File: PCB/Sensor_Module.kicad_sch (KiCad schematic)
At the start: 36 parts, among them J1 Conn_01x02_Pin, J2 Conn_01x01_Pin, J3 Conn_01x02_Pin, J4 Conn_01x02_Pin, J5 Conn_01x02_Pin, Q3 BSS123, Q4 BSS123, Q5 BSS123

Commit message: Changed Sensor Sheet Description
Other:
- company: (none) -> University of Cape Town
- title: (none) -> Sensor Module
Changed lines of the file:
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@@
 (kicad_sch (version 20230121) (generator eeschema)
   (paper "A4")
+  (title_block
+    (title "Sensor Module")
+    (date "2023-03-12")
+    (company "University of Cape Town")
+    (comment 1 "Author: Simon Carthew")
+    (comment 2 "v0.0")
+  )
   (junction (at 162.56 62.23) (diameter 0) (color 0 0 0 0)
   )

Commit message: Merging Fixed
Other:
- note added: "BI-DIRECTIONAL LOGIC LEVEL SHIFTING"
- moved on the sheet: C?, J2, J5, R?, U?

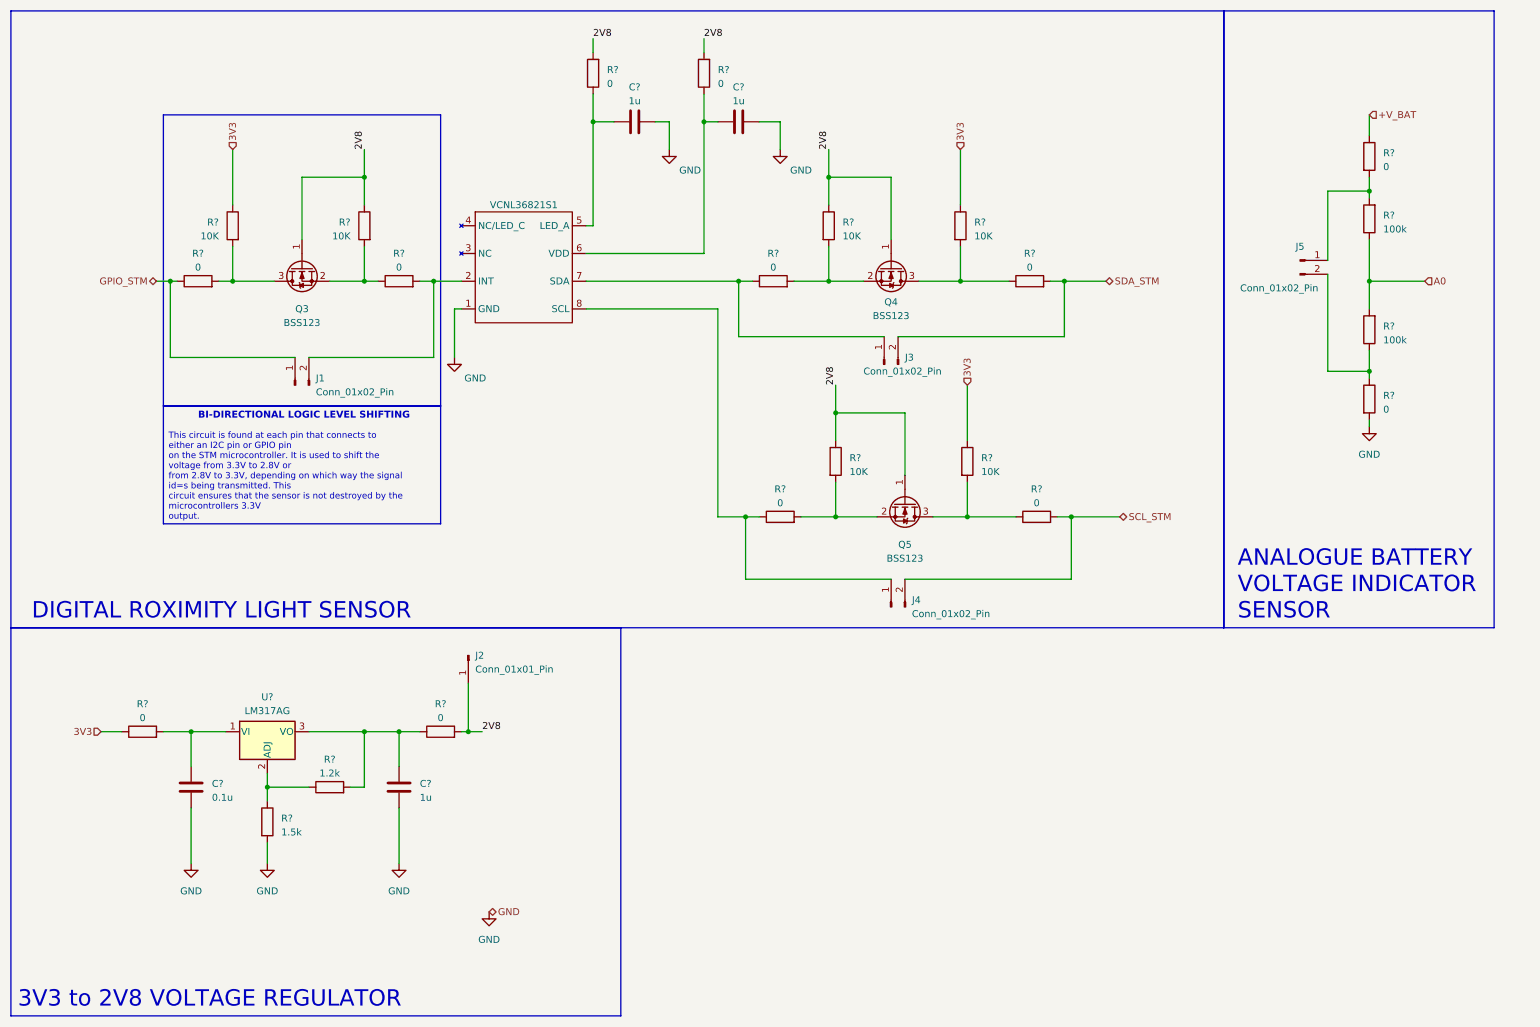
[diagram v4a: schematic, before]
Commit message: Changed Sensor and added hierachiel sheet
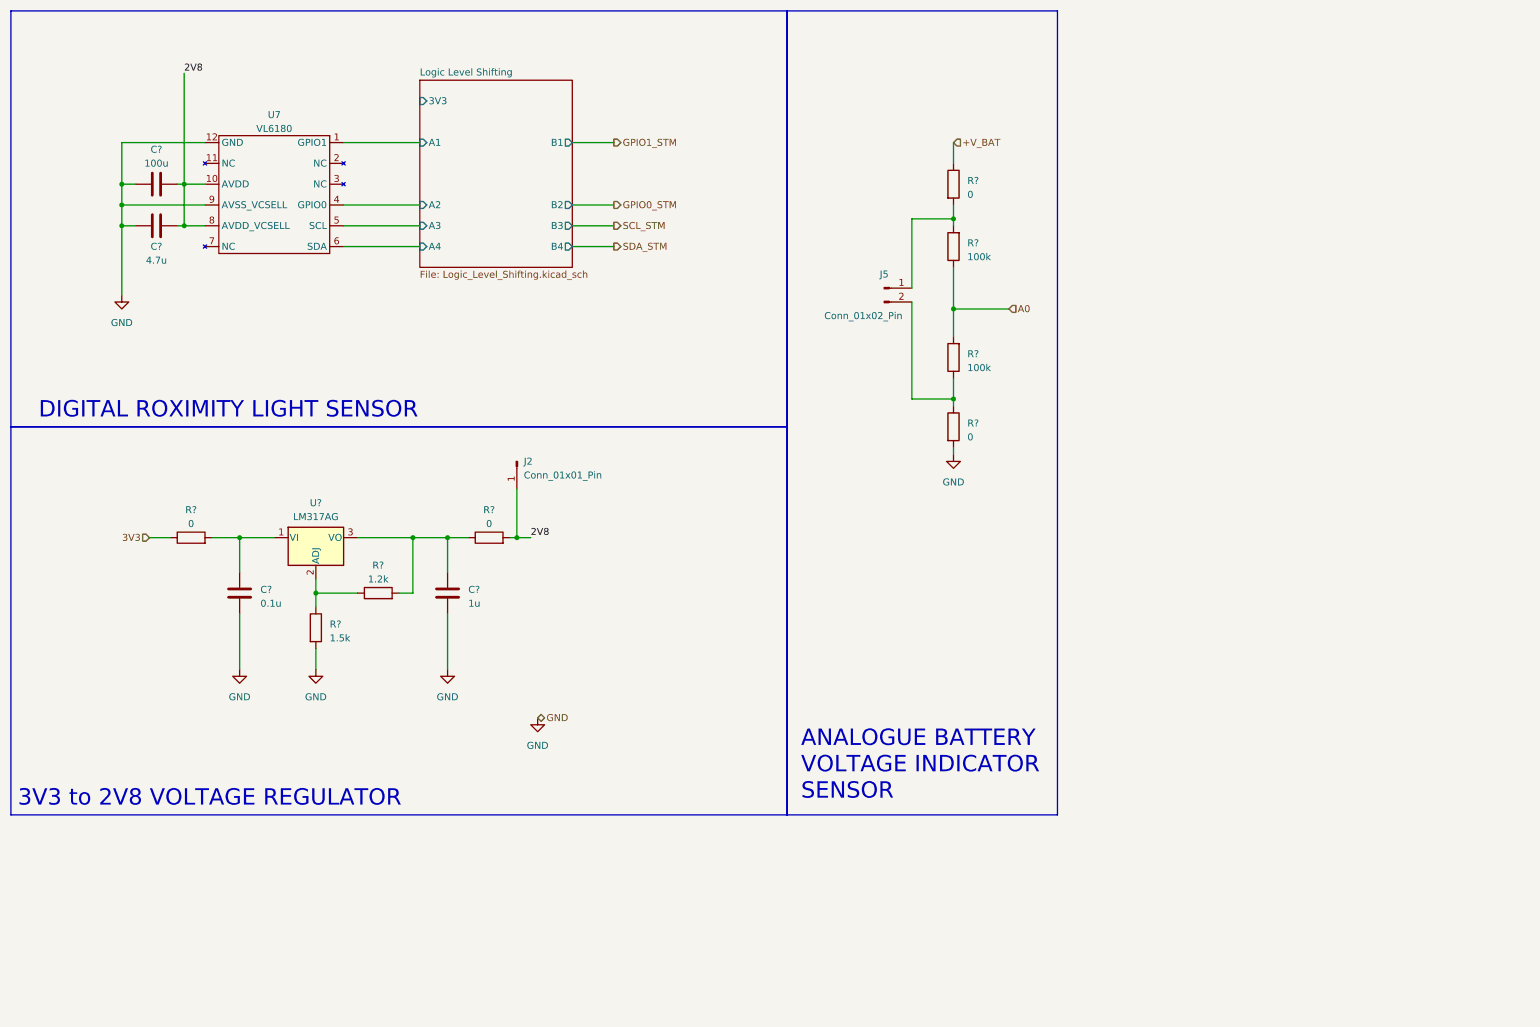
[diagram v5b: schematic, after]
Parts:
- removed C? (x2): 1u, symbol Device:C
- removed J1, J3, J4: Conn_01x02_Pin, symbol Connector:Conn_01x02_Pin
- removed Q3, Q4, Q5: BSS123, Package_TO_SOT_SMD:SOT-23, symbol Transistor_FET:BSS123
- removed R? (x6): 10K, symbol Device:R
- removed R? (x8): 0, symbol Device:R
- removed VCNL36821S1: ~, symbol Proximity Sensor:VCNL36821S
- added C?: 100u, symbol Device:C
- added C?: 4.7u, symbol Device:C
- added U7: VL6180, symbol Proximity Sensor:VL6180
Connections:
- net 2V8: now also C?.1, C?.1, U7.10 (AVDD), U7.8 (AVDD_VCSELL)
- net GND: now also C?.2, C?.2, U7.12 (GND), U7.9 (AVSS_VCSELL)
- new net Logic Level Shifting/A1: U7.1 (GPIO1)
- new net Logic Level Shifting/A2: U7.4 (GPIO0)
- new net Logic Level Shifting/A3: U7.5 (SCL)
- new net Logic Level Shifting/A4: U7.6 (SDA)
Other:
- added sheet Logic Level Shifting (Logic_Level_Shifting.kicad_sch)
- note removed: "BI-DIRECTIONAL LOGIC LEVEL SHIFTING"
- moved on the sheet: C?, J2, J5, R?, U?

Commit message: Merging commit
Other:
- moved on the sheet: J5, R?
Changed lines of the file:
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@@
     (comment 2 "v0.0")
   )
-  (junction (at 185.42 67.31) (diameter 0) (color 0 0 0 0)
+  (junction (at 184.15 85.09) (diameter 0) (color 0 0 0 0)
   )
   (junction (at 44.45 44.45) (diameter 0) (color 0 0 0 0)
@@
   (junction (at 33.02 48.26) (diameter 0) (color 0 0 0 0)
   )
-  (junction (at 185.42 50.8) (diameter 0) (color 0 0 0 0)
-  )
-  (junction (at 185.42 83.82) (diameter 0) (color 0 0 0 0)
+  (junction (at 184.15 68.58) (diameter 0) (color 0 0 0 0)
+  )
+  (junction (at 184.15 101.6) (diameter 0) (color 0 0 0 0)
   )
   (junction (at 44.45 52.07) (diameter 0) (color 0 0 0 0)
@@
     (stroke (width 0) (type default))
   )
-  (wire (pts (xy 185.42 83.82) (xy 185.42 85.09))
+  (wire (pts (xy 184.15 101.6) (xy 184.15 102.87))
     (stroke (width 0) (type default))
   )
@@
     (stroke (width 0) (type default))
   )
-  (wire (pts (xy 185.42 59.69) (xy 185.42 67.31))
+  (wire (pts (xy 184.15 77.47) (xy 184.15 85.09))
     (stroke (width 0) (type default))
   )
@@
     (stroke (width 0) (type default))
   )
-  (wire (pts (xy 177.8 50.8) (xy 177.8 63.5))
-    (stroke (width 0) (type default))
-  )
-  (wire (pts (xy 177.8 83.82) (xy 177.8 66.04))
+  (wire (pts (xy 176.53 68.58) (xy 176.53 81.28))
+    (stroke (width 0) (type default))
+  )
+  (wire (pts (xy 176.53 101.6) (xy 176.53 83.82))
     (stroke (width 0) (type default))
   )
@@
     (stroke (width 0) (type default))
   )
-  (wire (pts (xy 185.42 48.26) (xy 185.42 50.8))
+  (wire (pts (xy 184.15 66.04) (xy 184.15 68.58))
     (stroke (width 0) (type default))
   )
@@
     (stroke (width 0) (type default))
   )
-  (wire (pts (xy 185.42 67.31) (xy 185.42 72.39))
+  (wire (pts (xy 184.15 85.09) (xy 184.15 90.17))
     (stroke (width 0) (type default))
   )
@@
     (stroke (width 0) (type default))
   )
+  (wire (pts (xy 80.01 22.86) (xy 80.01 29.21))
+    (stroke (width 0) (type default))
+  )
+  (wire (pts (xy 87.63 29.21) (xy 80.01 29.21))
+    (stroke (width 0) (type default))
+  )
   (wire (pts (xy 68.58 119.38) (xy 68.58 121.92))
     (stroke (width 0) (type default))
   )
-  (wire (pts (xy 185.42 50.8) (xy 185.42 52.07))
+  (wire (pts (xy 184.15 68.58) (xy 184.15 69.85))
     (stroke (width 0) (type default))
   )
@@
     (stroke (width 0) (type default))
   )
-  (wire (pts (xy 185.42 83.82) (xy 177.8 83.82))
-    (stroke (width 0) (type default))
-  )
-  (wire (pts (xy 185.42 67.31) (xy 195.58 67.31))
+  (wire (pts (xy 184.15 101.6) (xy 176.53 101.6))
+    (stroke (width 0) (type default))
+  )
+  (wire (pts (xy 184.15 85.09) (xy 194.31 85.09))
     (stroke (width 0) (type default))
   )
@@
     (stroke (width 0) (type default))
   )
-  (wire (pts (xy 185.42 80.01) (xy 185.42 83.82))
+  (wire (pts (xy 184.15 97.79) (xy 184.15 101.6))
     (stroke (width 0) (type default))
   )
@@
     (stroke (width 0) (type default))
   )
-  (wire (pts (xy 185.42 92.71) (xy 185.42 93.98))
+  (wire (pts (xy 184.15 110.49) (xy 184.15 111.76))
     (stroke (width 0) (type default))
   )
@@
     (stroke (width 0) (type default))
   )
-  (wire (pts (xy 185.42 50.8) (xy 177.8 50.8))
+  (wire (pts (xy 184.15 68.58) (xy 176.53 68.58))
     (stroke (width 0) (type default))
   )
@@
     (stroke (width 0) (type default))
   )
-  (wire (pts (xy 185.42 36.83) (xy 185.42 40.64))
+  (wire (pts (xy 184.15 54.61) (xy 184.15 58.42))
     (stroke (width 0) (type default))
   )
@@
     (effects (font (size 1.27 1.27)) (justify left))
   )
-  (hierarchical_label "A0" (shape input) (at 195.58 67.31 0) (fields_autoplaced)
+  (hierarchical_label "A0" (shape input) (at 194.31 85.09 0) (fields_autoplaced)
     (effects (font (size 1.27 1.27)) (justify left))
   )
-  (hierarchical_label "+V_BAT" (shape input) (at 185.42 36.83 0) (fields_autoplaced)
+  (hierarchical_label "+V_BAT" (shape input) (at 184.15 54.61 90) (fields_autoplaced)
     (effects (font (size 1.27 1.27)) (justify left))
   )
@@
     (effects (font (size 1.27 1.27)) (justify left))
   )
-  (symbol (lib_id "power:GND") (at 185.42 93.98 0) (unit 1)
-    (in_bom yes) (on_board yes) (dnp no) (fields_autoplaced)
-    (property "Reference" "#PWR?" (at 185.42 100.33 0)
-      (effects (font (size 1.27 1.27)) hide)
-    )
-    (property "Value" "GND" (at 185.42 99.06 0)
-      (effects (font (size 1.27 1.27)))
-    )
-    (property "Footprint" "" (at 185.42 93.98 0)
-      (effects (font (size 1.27 1.27)) hide)
-    )
-    (property "Datasheet" "" (at 185.42 93.98 0)
+  (hierarchical_label "3V3" (shape input) (at 80.01 22.86 90) (fields_autoplaced)
+    (effects (font (size 1.27 1.27)) (justify left))
+  )
+  (symbol (lib_id "power:GND") (at 184.15 111.76 0) (unit 1)
+    (in_bom yes) (on_board yes) (dnp no) (fields_autoplaced)
+    (property "Reference" "#PWR?" (at 184.15 118.11 0)
+      (effects (font (size 1.27 1.27)) hide)
+    )
+    (property "Value" "GND" (at 184.15 116.84 0)
+      (effects (font (size 1.27 1.27)))
+    )
+    (property "Footprint" "" (at 184.15 111.76 0)
+      (effects (font (size 1.27 1.27)) hide)
+    )
+    (property "Datasheet" "" (at 184.15 111.76 0)
       (effects (font (size 1.27 1.27)) hide)
     )
@@
     )
   )
-  (symbol (lib_id "Device:R") (at 185.42 76.2 180) (unit 1)
-    (in_bom yes) (on_board yes) (dnp no) (fields_autoplaced)
-    (property "Reference" "R?" (at 187.96 75.565 0)
+  (symbol (lib_id "Device:R") (at 184.15 93.98 180) (unit 1)
+    (in_bom yes) (on_board yes) (dnp no) (fields_autoplaced)
+    (property "Reference" "R?" (at 186.69 93.345 0)
       (effects (font (size 1.27 1.27)) (justify right))
     )
-    (property "Value" "100k" (at 187.96 78.105 0)
+    (property "Value" "100k" (at 186.69 95.885 0)
       (effects (font (size 1.27 1.27)) (justify right))
     )
-    (property "Footprint" "" (at 187.198 76.2 90)
-      (effects (font (size 1.27 1.27)) hide)
-    )
-    (property "Datasheet" "~" (at 185.42 76.2 0)
+    (property "Footprint" "" (at 185.928 93.98 90)
+      (effects (font (size 1.27 1.27)) hide)
+    )
+    (property "Datasheet" "~" (at 184.15 93.98 0)
       (effects (font (size 1.27 1.27)) hide)
     )
@@
     )
   )
-  (symbol (lib_id "Connector:Conn_01x02_Pin") (at 172.72 63.5 0) (unit 1)
+  (symbol (lib_id "Connector:Conn_01x02_Pin") (at 171.45 81.28 0) (unit 1)
     (in_bom yes) (on_board yes) (dnp no)
-    (property "Reference" "J5" (at 172.72 60.96 0)
-      (effects (font (size 1.27 1.27)))
-    )
-    (property "Value" "Conn_01x02_Pin" (at 168.91 68.58 0)
-      (effects (font (size 1.27 1.27)))
-    )
-    (property "Footprint" "" (at 172.72 63.5 0)
-      (effects (font (size 1.27 1.27)) hide)
-    )
-    (property "Datasheet" "~" (at 172.72 63.5 0)
+    (property "Reference" "J5" (at 171.45 78.74 0)
+      (effects (font (size 1.27 1.27)))
+    )
+    (property "Value" "Conn_01x02_Pin" (at 167.64 86.36 0)
+      (effects (font (size 1.27 1.27)))
+    )
+    (property "Footprint" "" (at 171.45 81.28 0)
+      (effects (font (size 1.27 1.27)) hide)
+    )
+    (property "Datasheet" "~" (at 171.45 81.28 0)
       (effects (font (size 1.27 1.27)) hide)
     )
@@
     )
   )
-  (symbol (lib_id "Device:R") (at 185.42 44.45 0) (unit 1)
-    (in_bom yes) (on_board yes) (dnp no) (fields_autoplaced)
-    (property "Reference" "R?" (at 187.96 43.815 0)
+  (symbol (lib_id "Device:R") (at 184.15 62.23 0) (unit 1)
+    (in_bom yes) (on_board yes) (dnp no) (fields_autoplaced)
+    (property "Reference" "R?" (at 186.69 61.595 0)
       (effects (font (size 1.27 1.27)) (justify left))
     )
-    (property "Value" "0" (at 187.96 46.355 0)
+    (property "Value" "0" (at 186.69 64.135 0)
       (effects (font (size 1.27 1.27)) (justify left))
     )
-    (property "Footprint" "" (at 183.642 44.45 90)
-      (effects (font (size 1.27 1.27)) hide)
-    )
-    (property "Datasheet" "~" (at 185.42 44.45 0)
+    (property "Footprint" "" (at 182.372 62.23 90)
+      (effects (font (size 1.27 1.27)) hide)
+    )
+    (property "Datasheet" "~" (at 184.15 62.23 0)
       (effects (font (size 1.27 1.27)) hide)
     )
@@
     )
   )
-  (symbol (lib_id "Device:R") (at 185.42 88.9 0) (unit 1)
-    (in_bom yes) (on_board yes) (dnp no) (fields_autoplaced)
-    (property "Reference" "R?" (at 187.96 88.265 0)
+  (symbol (lib_id "Device:R") (at 184.15 106.68 0) (unit 1)
+    (in_bom yes) (on_board yes) (dnp no) (fields_autoplaced)
+    (property "Reference" "R?" (at 186.69 106.045 0)
       (effects (font (size 1.27 1.27)) (justify left))
     )
-    (property "Value" "0" (at 187.96 90.805 0)
+    (property "Value" "0" (at 186.69 108.585 0)
       (effects (font (size 1.27 1.27)) (justify left))
     )
-    (property "Footprint" "" (at 183.642 88.9 90)
-      (effects (font (size 1.27 1.27)) hide)
-    )
-    (property "Datasheet" "~" (at 185.42 88.9 0)
+    (property "Footprint" "" (at 182.372 106.68 90)
+      (effects (font (size 1.27 1.27)) hide)
+    )
+    (property "Datasheet" "~" (at 184.15 106.68 0)
       (effects (font (size 1.27 1.27)) hide)
     )
@@
     )
   )
-  (symbol (lib_id "Device:R") (at 185.42 55.88 180) (unit 1)
-    (in_bom yes) (on_board yes) (dnp no) (fields_autoplaced)
-    (property "Reference" "R?" (at 187.96 55.245 0)
+  (symbol (lib_id "Device:R") (at 184.15 73.66 180) (unit 1)
+    (in_bom yes) (on_board yes) (dnp no) (fields_autoplaced)
+    (property "Reference" "R?" (at 186.69 73.025 0)
       (effects (font (size 1.27 1.27)) (justify right))
     )
-    (property "Value" "100k" (at 187.96 57.785 0)
+    (property "Value" "100k" (at 186.69 75.565 0)
       (effects (font (size 1.27 1.27)) (justify right))
     )
-    (property "Footprint" "" (at 187.198 55.88 90)
-      (effects (font (size 1.27 1.27)) hide)
-    )
-    (property "Datasheet" "~" (at 185.42 55.88 0)
-      (effects (font (size 1.27 1.27)) hide)
-    )
+    (property "Footprint" "" (at 185.928 73.66 90)
+      (effects (font (size 1.27 1.27)) hide)
+    )
+    (property "Datasheet" "~" (at 184.15 73.66 0)
+      (effects (font (size 1.27 1.27)) hide)
+    )
